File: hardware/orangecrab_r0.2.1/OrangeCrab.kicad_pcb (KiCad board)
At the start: 6 copper layers, 50.8 x 22.9 mm, 163 parts, among them J1 Conn_01x12_Male, J2 Conn_01x16_Male, J3 USB_C_Receptacle_USB2.0, J4 MicroSd, J5 JST, J6 Conn_01x05_Male, SW1 SW_Push, U1 TLV62569DRL, U10 NCP115-2.5, U2 TLV62569DRL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

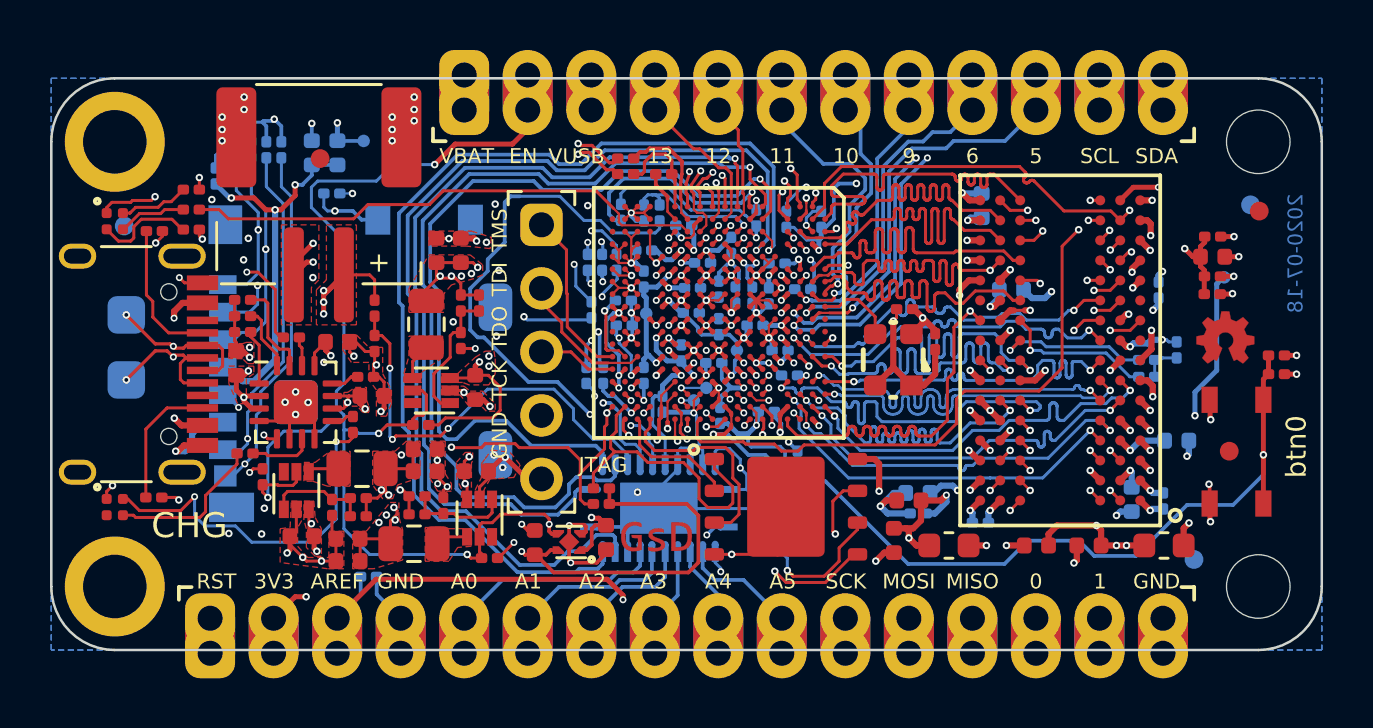
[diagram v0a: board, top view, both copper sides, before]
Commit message: Replaced from ECP5U-25 to ECP5UM-25 pinout and added SerDes banks
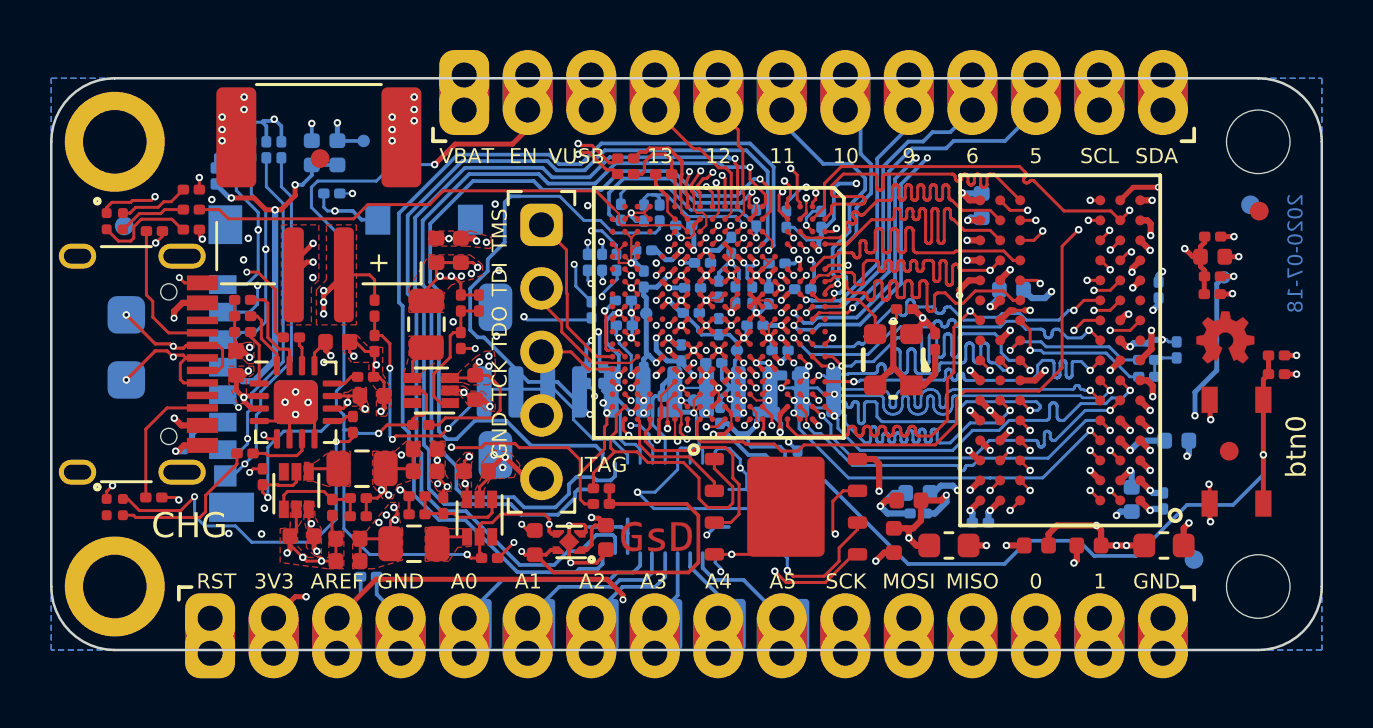
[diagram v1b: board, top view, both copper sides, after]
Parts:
- U3: value LFE5U-25F-8MG285C -> LFE5UM-25F-8MG285C
- U9: footprint Package_DFN_QFN:Texas_RGY_R-PVQFN-N24_EP2.05x3.1mm -> Package_SO:SOIC-24W_7.5x15.4mm_P1.27mm
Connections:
- net Net-(U3-PadV11) renamed SFP_TXN0
- net Net-(U3-PadV12) renamed SFP_TXP0
- net Net-(U3-PadV2) renamed SFP_TXN1
- net Net-(U3-PadV3) renamed SFP_TXP1
- D2 pad 4: Net-(D2-Pad4) -> unconnected-(D2-BK-Pad4)
- J3 pad A8: Net-(J3-PadA8) -> unconnected-(J3-SBU1-PadA8)
- J3 pad B8: Net-(J3-PadB8) -> unconnected-(J3-SBU2-PadB8)
- U1 pad 6: Net-(U1-Pad6) -> unconnected-(U1-NC-Pad6)
- U2 pad 6: Net-(U2-Pad6) -> unconnected-(U2-NC-Pad6)
- U3 pad A10: Net-(U3-PadA10) -> unconnected-(U3A-PT27B/PCLKC0_1-PadA10)
- U3 pad A11: Net-(U3-PadA11) -> unconnected-(U3A-PT27A/PCLKT0_1-PadA11)
- U3 pad B11: Net-(U3-PadB11) -> unconnected-(U3A-PT4A-PadB11)
- U3 pad C11: Net-(U3-PadC11) -> unconnected-(U3A-PT4B-PadC11)
- U3 pad H18: Net-(U3-PadH18) -> unconnected-(U3E-PL38D-PadH18)
- U3 pad P10: GND -> Net-(U3L-VCCA0-PadP10)
- U3 pad P5: GND -> Net-(U3L-VCCAUXA0-PadP5)
- U3 pad R10: GND -> Net-(U3L-VCCA0-PadP10)
- U3 pad R16: Net-(U3-PadR16) -> unconnected-(U3G-PB18A/WRITEN-PadR16)
- U3 pad R3: GND -> Net-(U3L-VCCAUXA0-PadP5)
- U3 pad T1: GND -> REFCLKN0
- U3 pad T5: GND -> P3.3V
- U3 pad U1: GND -> REFCLKP0
- U3 pad U12: GND -> P3.3V
- U3 pad U15: Net-(U3-PadU15) -> unconnected-(U3H-DONE-PadU15)
- U3 pad U6: GND -> P3.3V
- U3 pad U8: GND -> P3.3V
- U3 pad V16: Net-(U3-PadV16) -> unconnected-(U3H-INITN-PadV16)
- U3 pad V5: GND -> SFP_RXP1
- U3 pad V6: GND -> SFP_RXN1
- U3 pad V8: GND -> SFP_RXN0
- U3 pad V9: GND -> SFP_RXP0
- U7 pad 6: Net-(U7-Pad6) -> unconnected-(U7-NC-Pad6)
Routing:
- net GND: track 250.6 -> 243.2 mm, vias 141 -> 139
- net P3.3V: track 86.1 -> 86.5 mm, vias 20 -> 21
- net Net-(U3L-VCCAUXA0-PadP5): track 0.00 -> 0.01 mm, vias 0 -> 1
